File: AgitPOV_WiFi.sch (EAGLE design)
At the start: 33 parts

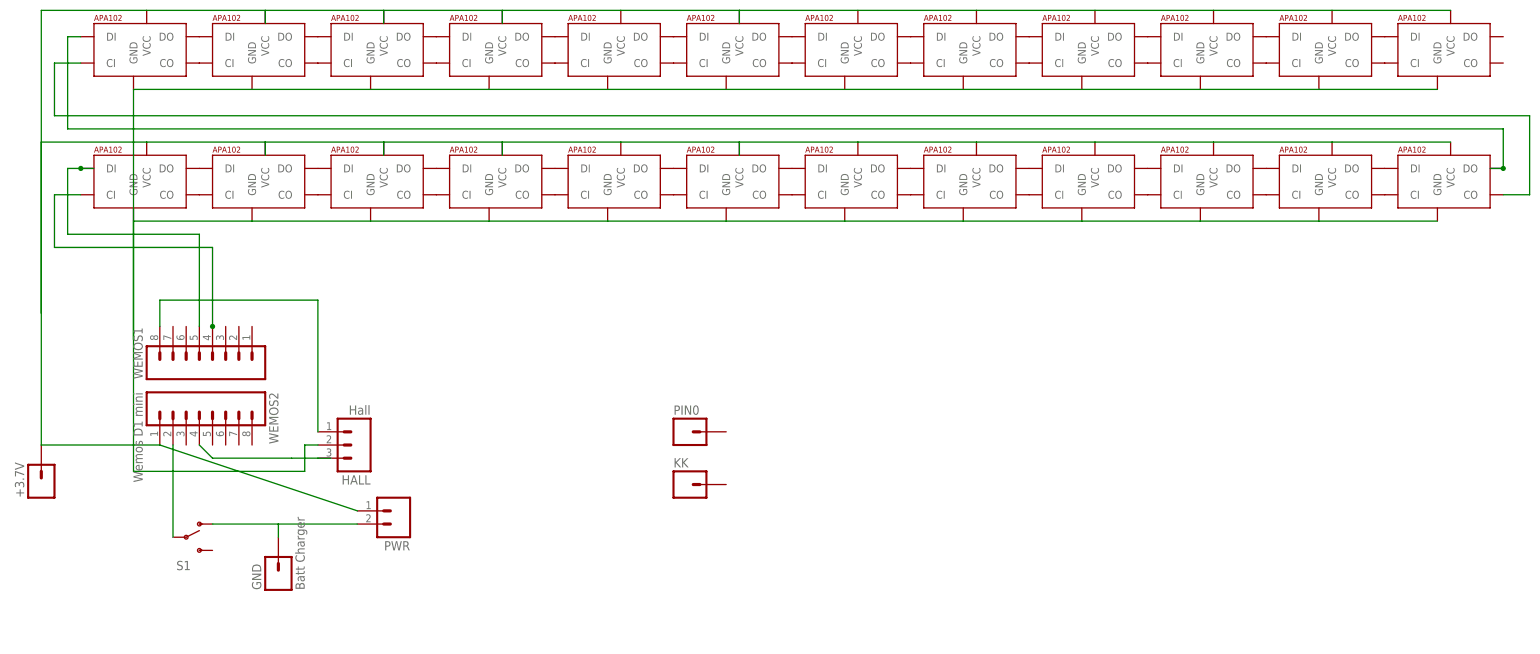
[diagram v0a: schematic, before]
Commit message: With an option (untested) of an accelerometer.
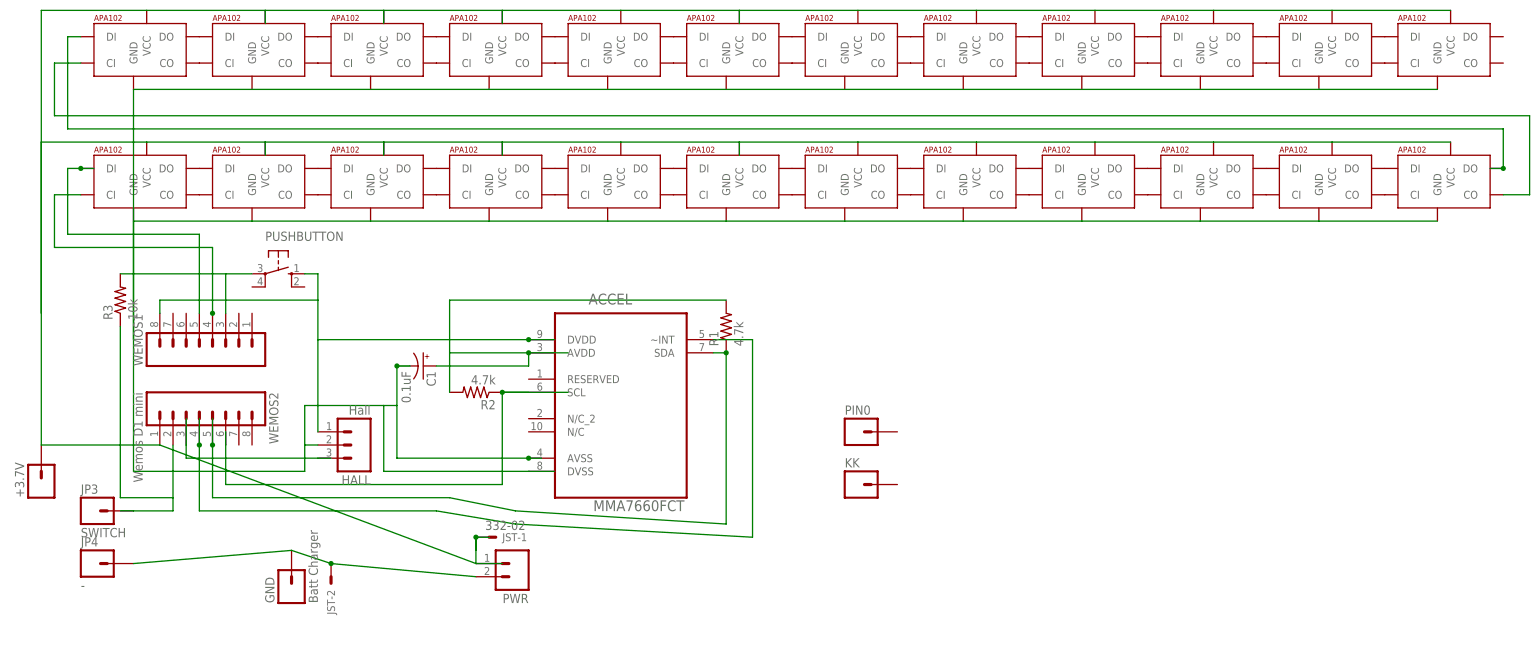
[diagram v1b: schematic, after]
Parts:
- removed S1: (no value), SparkFun-Electromechanical:SWITCH-SPDT-SMD-A
- added ACCEL: MMA7660FCT, Freescale_By_element14_Batch_1:MMA7660FCT
- added C1: 0.1uF, SparkFun-Capacitors:10UF-16V-10%(TANT)
- added JP3: SWITCH, SparkFun-Connectors:M01PTH
- added JP4: -, SparkFun-Connectors:M01PTH
- added JST: 332-02, con-garry:332-02
- added PUSHBUTTON: (no value), switch-omron:10-XX
- added R1, R2: 4.7k, SparkFun-Resistors:RESISTOR1206
- added R3: 10k, SparkFun-Resistors:RESISTOR1206
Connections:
- removed net CH_PD: HALL.1, WEMOS1.8
- removed net D3: HALL.3, WEMOS2.4
- new net +3.3V: ACCEL.AVDD, ACCEL.DVDD, C1.+, HALL.1, PUSHBUTTON.S, R1.2, R2.2, WEMOS1.8
- new net N$1: HALL.3, WEMOS2.3
- new net N$5: ACCEL.SCL, R2.1, WEMOS2.6
- new net N$65: ACCEL.SDA, R1.1, WEMOS2.5
- new net N$67: ACCEL.~INT, WEMOS2.4
- new net PULLDOWN: PUSHBUTTON.P, R3.2, WEMOS1.3
- net 5V: now also JST-1.S
- net GND: now also ACCEL.AVSS, ACCEL.DVSS, C1.-, JP3.1, R3.1; no longer S1.P
- net N$41: now also JP4.1, JST-2.S; no longer S1.O
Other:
- moved on the sheet: GND, KK, PIN0, PWR, WEMOS1

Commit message: Tout à sa place
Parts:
- removed +3.7V: (no value), SparkFun-Connectors:M01PTH
- removed JP3: SWITCH, SparkFun-Connectors:M01PTH
- removed JP4: -, SparkFun-Connectors:M01PTH
- removed PWR: (no value), SparkFun-Connectors:M02LOCK_LONGPADS
- added BATT: (no value), SparkFun-Connectors:M02LOCK_LONGPADS
- added BATT+: (no value), SparkFun-Connectors:M01PTH
- added JP-GND: SWITCH, SparkFun-Connectors:M01PTH
- added JP-GNDE: -, SparkFun-Connectors:M01PTH
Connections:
- removed net 5V1: DEL13.VCC, DEL15.VCC, DEL16.VCC, DEL17.VCC, DEL18.VCC, DEL19.VCC, DEL20.VCC, DEL21.VCC, DEL22.VCC, DEL23.VCC, DEL24.VCC, FFFFF.VCC
- removed net GND1: DEL13.GND, DEL15.GND, DEL16.GND, DEL17.GND, DEL18.GND, DEL19.GND, DEL20.GND, DEL21.GND, DEL22.GND, DEL23.GND, DEL24.GND, FFFFF.GND
- removed net N$41: GND.1, JP4.1, JST-2.S, PWR.2
- new net ENTREEGND: BATT.1, GND.1, JP-GNDE.1, JST-1.S
- net 5V: now also BATT+.1, BATT.2, DEL13.VCC, DEL15.VCC, DEL16.VCC, DEL17.VCC, DEL18.VCC, DEL19.VCC, DEL20.VCC, DEL21.VCC, DEL22.VCC, DEL23.VCC, DEL24.VCC, FFFFF.VCC, JST-2.S; no longer +3.7V.1, JST-1.S, PWR.1
- net GND: now also DEL13.GND, DEL15.GND, DEL16.GND, DEL17.GND, DEL18.GND, DEL19.GND, DEL20.GND, DEL21.GND, DEL22.GND, DEL23.GND, DEL24.GND, FFFFF.GND, JP-GND.1; no longer JP3.1
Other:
- moved on the sheet: GND, JST-1, JST-2, PIN0, WEMOS2

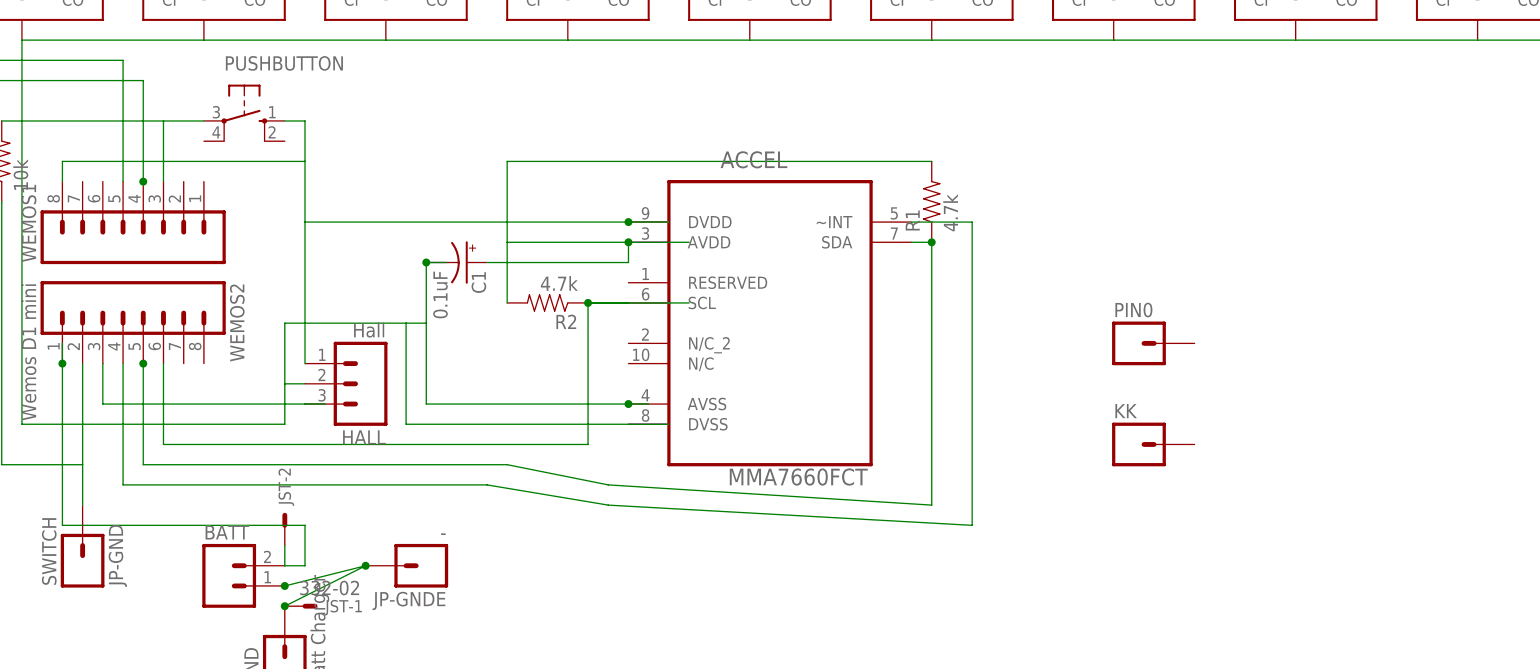
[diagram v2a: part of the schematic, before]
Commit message: added a capacitor for the accelerometer, DRChecked
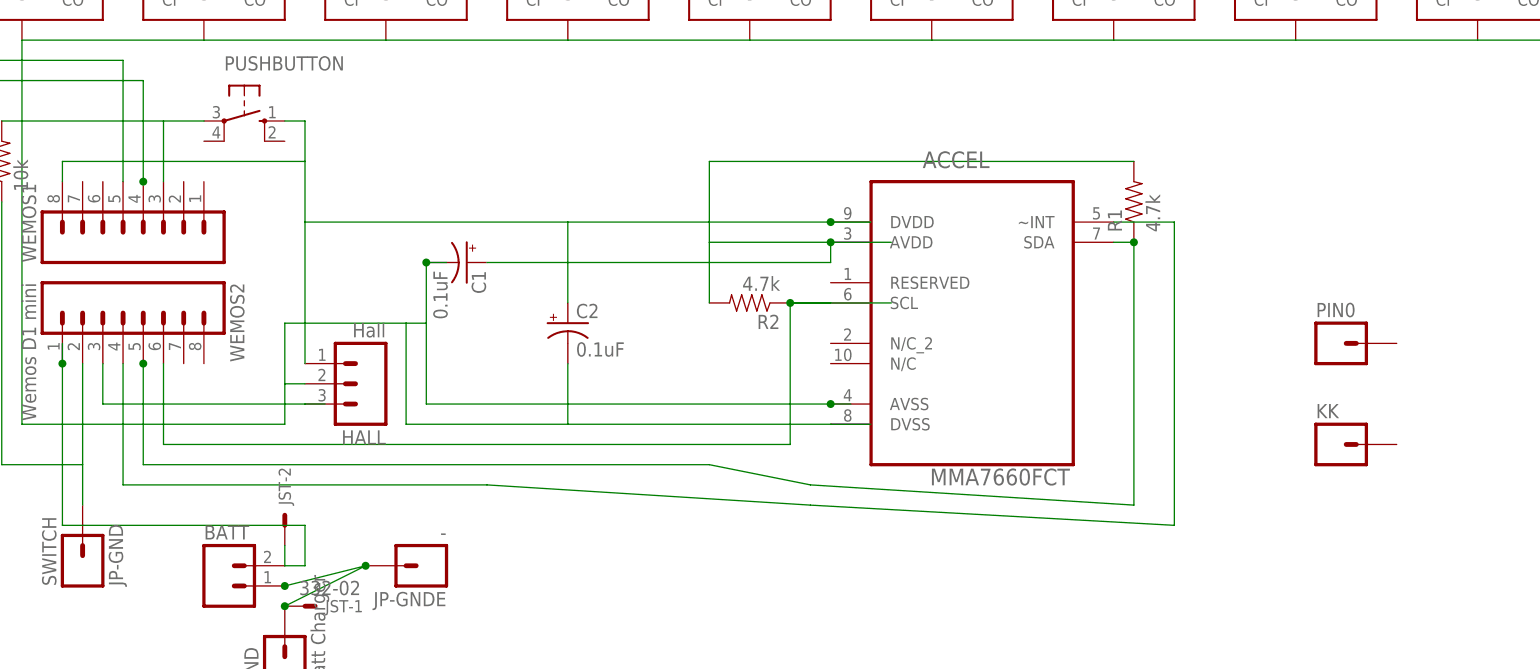
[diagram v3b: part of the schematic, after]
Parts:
- added C2: 0.1uF, SparkFun-Capacitors:10UF-16V-10%(TANT)
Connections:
- net +3.3V: now also C2.+
- net GND: now also C2.-
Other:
- moved on the sheet: ACCEL, KK, PIN0, R1, R2
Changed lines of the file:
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@@
 <part name="JP-GNDE" library="SparkFun-Connectors" deviceset="M01" device="PTH" value="-"/>
 <part name="R3" library="SparkFun-Resistors" deviceset="RESISTOR" device="1206" value="10k"/>
+<part name="C2" library="SparkFun-Capacitors" deviceset="10UF-16V-10%(TANT)" device="" value="0.1uF"/>
 </parts>
 <sheets>
@@
 <instance part="WEMOS2" gate="G$1" x="40.64" y="40.64" rot="R270"/>
 <instance part="HALL" gate="G$1" x="71.12" y="33.02" rot="R180"/>
-<instance part="PIN0" gate="G$1" x="167.64" y="38.1"/>
-<instance part="KK" gate="G$1" x="167.64" y="25.4"/>
+<instance part="PIN0" gate="G$1" x="193.04" y="38.1"/>
+<instance part="KK" gate="G$1" x="193.04" y="25.4"/>
 <instance part="GND" gate="G$1" x="60.96" y="-2.54" rot="R90"/>
 <instance part="BATT+" gate="G$1" x="15.24" y="48.26" rot="R180"/>
@@
 <instance part="DEL23" gate="G$1" x="259.08" y="106.68"/>
 <instance part="DEL24" gate="G$1" x="281.94" y="106.68"/>
-<instance part="ACCEL" gate="A" x="121.92" y="43.18"/>
-<instance part="R1" gate="G$1" x="142.24" y="55.88" rot="R90"/>
-<instance part="R2" gate="G$1" x="93.98" y="43.18" rot="R180"/>
+<instance part="ACCEL" gate="A" x="147.32" y="43.18"/>
+<instance part="R1" gate="G$1" x="167.64" y="55.88" rot="R90"/>
+<instance part="R2" gate="G$1" x="119.38" y="43.18" rot="R180"/>
 <instance part="C1" gate="G$1" x="83.82" y="48.26" rot="R270"/>
 <instance part="JST" gate="-1" x="63.5" y="5.08" smashed="yes">
@@
 <instance part="JP-GNDE" gate="G$1" x="78.74" y="10.16" rot="R180"/>
 <instance part="R3" gate="G$1" x="25.4" y="60.96" rot="R90"/>
+<instance part="C2" gate="G$1" x="96.52" y="40.64"/>
 </instances>
 <busses>
@@
 <wire x1="27.94" y1="27.94" x2="35.56" y2="27.94" width="0.1524" layer="91"/>
 <wire x1="60.96" y1="33.02" x2="60.96" y2="40.64" width="0.1524" layer="91"/>
-<wire x1="78.74" y1="30.48" x2="104.14" y2="30.48" width="0.1524" layer="91"/>
+<wire x1="78.74" y1="30.48" x2="129.54" y2="30.48" width="0.1524" layer="91"/>
 <wire x1="60.96" y1="40.64" x2="76.2" y2="40.64" width="0.1524" layer="91"/>
 <wire x1="76.2" y1="40.64" x2="78.74" y2="40.64" width="0.1524" layer="91"/>
 <wire x1="78.74" y1="40.64" x2="78.74" y2="30.48" width="0.1524" layer="91"/>
-<wire x1="104.14" y1="30.48" x2="106.68" y2="30.48" width="0.1524" layer="91"/>
+<wire x1="129.54" y1="30.48" x2="132.08" y2="30.48" width="0.1524" layer="91"/>
 <pinref part="ACCEL" gate="A" pin="AVSS"/>
-<junction x="104.14" y="30.48"/>
+<junction x="129.54" y="30.48"/>
 <wire x1="81.28" y1="48.26" x2="78.74" y2="48.26" width="0.1524" layer="91"/>
 <wire x1="78.74" y1="48.26" x2="78.74" y2="40.64" width="0.1524" layer="91"/>
@@
 <junction x="78.74" y="48.26"/>
 <pinref part="ACCEL" gate="A" pin="DVSS"/>
-<wire x1="104.14" y1="27.94" x2="109.22" y2="27.94" width="0.1524" layer="91"/>
-<wire x1="104.14" y1="27.94" x2="76.2" y2="27.94" width="0.1524" layer="91"/>
+<wire x1="129.54" y1="27.94" x2="134.62" y2="27.94" width="0.1524" layer="91"/>
+<wire x1="129.54" y1="27.94" x2="96.52" y2="27.94" width="0.1524" layer="91"/>
+<wire x1="96.52" y1="27.94" x2="76.2" y2="27.94" width="0.1524" layer="91"/>
 <wire x1="76.2" y1="27.94" x2="76.2" y2="40.64" width="0.1524" layer="91"/>
 <pinref part="JP-GND" gate="G$1" pin="1"/>
@@
 <wire x1="25.4" y1="22.86" x2="25.4" y2="55.88" width="0.1524" layer="91"/>
 <pinref part="R3" gate="G$1" pin="1"/>
+<pinref part="C2" gate="G$1" pin="-"/>
+<wire x1="96.52" y1="35.56" x2="96.52" y2="27.94" width="0.1524" layer="91"/>
 </segment>
 <segment>
@@
 <wire x1="63.5" y1="60.96" x2="63.5" y2="53.34" width="0.1524" layer="91"/>
 <wire x1="63.5" y1="53.34" x2="63.5" y2="35.56" width="0.1524" layer="91"/>
-<wire x1="109.22" y1="53.34" x2="104.14" y2="53.34" width="0.1524" layer="91"/>
-<wire x1="88.9" y1="53.34" x2="88.9" y2="50.8" width="0.1524" layer="91"/>
-<wire x1="88.9" y1="50.8" x2="104.14" y2="50.8" width="0.1524" layer="91"/>
+<wire x1="134.62" y1="53.34" x2="129.54" y2="53.34" width="0.1524" layer="91"/>
+<wire x1="114.3" y1="53.34" x2="114.3" y2="50.8" width="0.1524" layer="91"/>
+<wire x1="114.3" y1="50.8" x2="129.54" y2="50.8" width="0.1524" layer="91"/>
 <pinref part="ACCEL" gate="A" pin="DVDD"/>
-<junction x="104.14" y="53.34"/>
+<junction x="129.54" y="53.34"/>
 <pinref part="ACCEL" gate="A" pin="AVDD"/>
-<junction x="104.14" y="50.8"/>
-<wire x1="63.5" y1="53.34" x2="88.9" y2="53.34" width="0.1524" layer="91"/>
-<wire x1="88.9" y1="53.34" x2="104.14" y2="53.34" width="0.1524" layer="91"/>
+<junction x="129.54" y="50.8"/>
+<wire x1="63.5" y1="53.34" x2="96.52" y2="53.34" width="0.1524" layer="91"/>
+<wire x1="96.52" y1="53.34" x2="114.3" y2="53.34" width="0.1524" layer="91"/>
+<wire x1="114.3" y1="53.34" x2="129.54" y2="53.34" width="0.1524" layer="91"/>
 <pinref part="C1" gate="G$1" pin="+"/>
-<wire x1="111.76" y1="50.8" x2="104.14" y2="50.8" width="0.1524" layer="91"/>
-<wire x1="104.14" y1="50.8" x2="104.14" y2="48.26" width="0.1524" layer="91"/>
-<wire x1="104.14" y1="48.26" x2="86.36" y2="48.26" width="0.1524" layer="91"/>
+<wire x1="137.16" y1="50.8" x2="129.54" y2="50.8" width="0.1524" layer="91"/>
+<wire x1="129.54" y1="50.8" x2="129.54" y2="48.26" width="0.1524" layer="91"/>
+<wire x1="129.54" y1="48.26" x2="86.36" y2="48.26" width="0.1524" layer="91"/>
 <pinref part="R2" gate="G$1" pin="2"/>
-<wire x1="88.9" y1="43.18" x2="88.9" y2="50.8" width="0.1524" layer="91"/>
+<wire x1="114.3" y1="43.18" x2="114.3" y2="50.8" width="0.1524" layer="91"/>
 <pinref part="R1" gate="G$1" pin="2"/>
-<wire x1="142.24" y1="60.96" x2="88.9" y2="60.96" width="0.1524" layer="91"/>
-<wire x1="88.9" y1="53.34" x2="88.9" y2="60.96" width="0.1524" layer="91"/>
+<wire x1="167.64" y1="60.96" x2="114.3" y2="60.96" width="0.1524" layer="91"/>
+<wire x1="114.3" y1="53.34" x2="114.3" y2="60.96" width="0.1524" layer="91"/>
 <pinref part="PUSHBUTTON" gate="1" pin="S"/>
 <wire x1="60.96" y1="66.04" x2="63.5" y2="66.04" width="0.1524" layer="91"/>
 <wire x1="63.5" y1="66.04" x2="63.5" y2="60.96" width="0.1524" layer="91"/>
+<wire x1="96.52" y1="43.18" x2="96.52" y2="53.34" width="0.1524" layer="91"/>
+<pinref part="C2" gate="G$1" pin="+"/>
 </segment>
 </net>
@@
 <net name="N$5" class="0">
 <segment>
-<wire x1="111.76" y1="43.18" x2="99.06" y2="43.18" width="0.1524" layer="91"/>
-<wire x1="99.06" y1="43.18" x2="99.06" y2="25.4" width="0.1524" layer="91"/>
-<wire x1="99.06" y1="25.4" x2="45.72" y2="25.4" width="0.1524" layer="91"/>
+<wire x1="137.16" y1="43.18" x2="124.46" y2="43.18" width="0.1524" layer="91"/>
+<wire x1="124.46" y1="43.18" x2="124.46" y2="25.4" width="0.1524" layer="91"/>
+<wire x1="124.46" y1="25.4" x2="45.72" y2="25.4" width="0.1524" layer="91"/>
 <wire x1="45.72" y1="25.4" x2="45.72" y2="35.56" width="0.1524" layer="91"/>
 <pinref part="WEMOS2" gate="G$1" pin="6"/>
 <pinref part="ACCEL" gate="A" pin="SCL"/>
-<junction x="99.06" y="43.18"/>
+<junction x="124.46" y="43.18"/>
 <pinref part="R2" gate="G$1" pin="1"/>
-<wire x1="99.06" y1="43.18" x2="104.14" y2="43.18" width="0.1524" layer="91"/>
+<wire x1="124.46" y1="43.18" x2="129.54" y2="43.18" width="0.1524" layer="91"/>
 </segment>
 </net>
@@
 <segment>
 <wire x1="43.18" y1="35.56" x2="43.18" y2="22.86" width="0.1524" layer="91"/>
-<wire x1="43.18" y1="22.86" x2="88.9" y2="22.86" width="0.1524" layer="91"/>
-<wire x1="88.9" y1="22.86" x2="101.6" y2="20.32" width="0.1524" layer="91"/>
-<wire x1="101.6" y1="20.32" x2="142.24" y2="17.78" width="0.1524" layer="91"/>
-<wire x1="142.24" y1="17.78" x2="142.24" y2="50.8" width="0.1524" layer="91"/>
-<wire x1="142.24" y1="50.8" x2="139.7" y2="50.8" width="0.1524" layer="91"/>
+<wire x1="43.18" y1="22.86" x2="114.3" y2="22.86" width="0.1524" layer="91"/>
+<wire x1="114.3" y1="22.86" x2="127" y2="20.32" width="0.1524" layer="91"/>
+<wire x1="127" y1="20.32" x2="167.64" y2="17.78" width="0.1524" layer="91"/>
+<wire x1="167.64" y1="17.78" x2="167.64" y2="50.8" width="0.1524" layer="91"/>
+<wire x1="167.64" y1="50.8" x2="165.1" y2="50.8" width="0.1524" layer="91"/>
 <pinref part="ACCEL" gate="A" pin="SDA"/>
 <pinref part="WEMOS2" gate="G$1" pin="5"/>
 <junction x="43.18" y="35.56"/>
 <pinref part="R1" gate="G$1" pin="1"/>
-<junction x="142.24" y="50.8"/>
+<junction x="167.64" y="50.8"/>
 </segment>
 </net>
 <net name="N$67" class="0">
 <segment>
-<wire x1="139.7" y1="53.34" x2="147.32" y2="53.34" width="0.1524" layer="91"/>
-<wire x1="147.32" y1="53.34" x2="147.32" y2="15.24" width="0.1524" layer="91"/>
-<wire x1="147.32" y1="15.24" x2="101.6" y2="17.78" width="0.1524" layer="91"/>
-<wire x1="101.6" y1="17.78" x2="86.36" y2="20.32" width="0.1524" layer="91"/>
+<wire x1="165.1" y1="53.34" x2="172.72" y2="53.34" width="0.1524" layer="91"/>
+<wire x1="172.72" y1="53.34" x2="172.72" y2="15.24" width="0.1524" layer="91"/>
+<wire x1="172.72" y1="15.24" x2="127" y2="17.78" width="0.1524" layer="91"/>
+<wire x1="127" y1="17.78" x2="86.36" y2="20.32" width="0.1524" layer="91"/>
 <wire x1="86.36" y1="20.32" x2="40.64" y2="20.32" width="0.1524" layer="91"/>
 <wire x1="40.64" y1="20.32" x2="40.64" y2="35.56" width="0.1524" layer="91"/>

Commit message: proper ACCEL integration
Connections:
- net GND: now also ACCEL.RESERVED
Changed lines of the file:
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@@
 <wire x1="27.94" y1="27.94" x2="35.56" y2="27.94" width="0.1524" layer="91"/>
 <wire x1="60.96" y1="33.02" x2="60.96" y2="40.64" width="0.1524" layer="91"/>
-<wire x1="78.74" y1="30.48" x2="129.54" y2="30.48" width="0.1524" layer="91"/>
+<wire x1="78.74" y1="30.48" x2="109.22" y2="30.48" width="0.1524" layer="91"/>
+<wire x1="109.22" y1="30.48" x2="129.54" y2="30.48" width="0.1524" layer="91"/>
 <wire x1="60.96" y1="40.64" x2="76.2" y2="40.64" width="0.1524" layer="91"/>
 <wire x1="76.2" y1="40.64" x2="78.74" y2="40.64" width="0.1524" layer="91"/>
@@
 <pinref part="C2" gate="G$1" pin="-"/>
 <wire x1="96.52" y1="35.56" x2="96.52" y2="27.94" width="0.1524" layer="91"/>
+<wire x1="132.08" y1="45.72" x2="129.54" y2="45.72" width="0.1524" layer="91"/>
+<wire x1="129.54" y1="45.72" x2="109.22" y2="45.72" width="0.1524" layer="91"/>
+<wire x1="109.22" y1="45.72" x2="109.22" y2="30.48" width="0.1524" layer="91"/>
+<pinref part="ACCEL" gate="A" pin="RESERVED"/>
+<junction x="129.54" y="45.72"/>
 </segment>
 <segment>
